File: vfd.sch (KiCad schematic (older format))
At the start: 35 parts, among them Q1 AO3400A, Q13 TO-252, Q14 CJT04N15, Q2 AO3400A, T1 Wuerth 760390013, T2 Wuerth 760390013, T3 Wuerth 760390013, T4 Wuerth 760390013, U1 SN74AVC8T245PW, U4 MN12864K

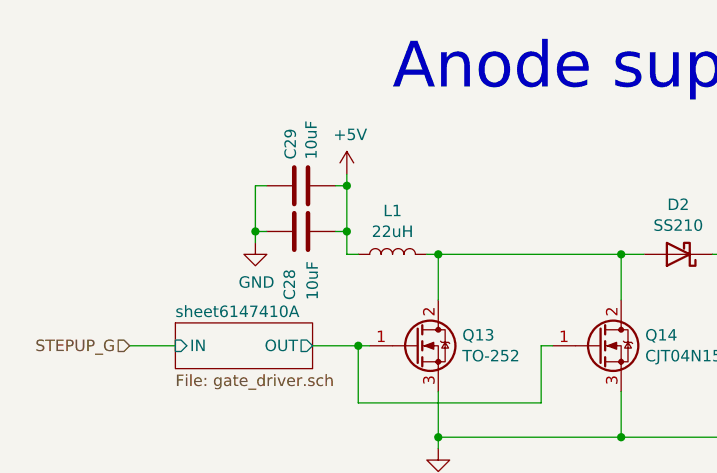
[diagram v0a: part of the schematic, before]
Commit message: Assign unique value to low voltage 0805 caps
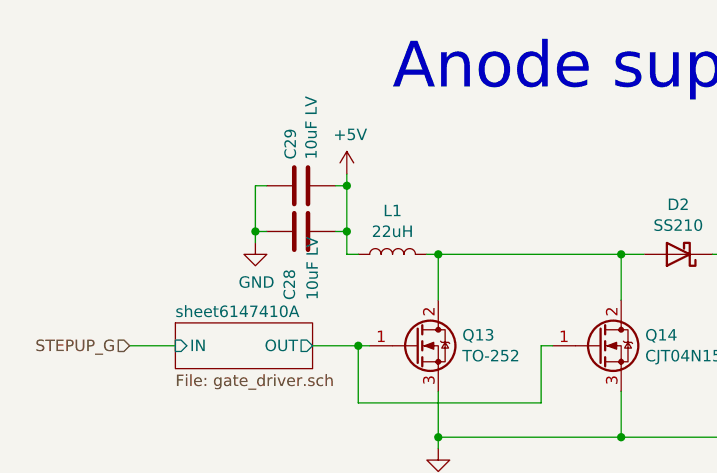
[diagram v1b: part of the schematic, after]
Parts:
- C28, C29: value 10uF -> 10uF LV
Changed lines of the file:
@@
-$Comp
-L Device:C C?
-U 1 1 60D56122
-P 2000 1450
-AR Path="/60B03476/60D3C691/60D56122" Ref="C?"  Part="1"
-AR Path="/60B03476/60D56122" Ref="C28"  Part="1"
-F 0 "C28" H 1700 1500 50  0000 L CNN
-F 1 "10uF" H 1700 1400 50  0000 L CNN
-F 2 "Capacitor_SMD:C_0805_2012Metric" H 2038 1300 50  0001 C CNN
-F 3 "~" H 2000 1450 50  0001 C CNN
-F 4 "C15850" V 2000 1450 50  0001 C CNN "LCSC"
-	1    2000 1450
-	0    -1   -1   0
-$EndComp
 $Comp
 L Device:C C?
@@
 AR Path="/60B03476/60D56129" Ref="C29"  Part="1"
 F 0 "C29" H 2115 1296 50  0000 L CNN
-F 1 "10uF" H 2115 1205 50  0000 L CNN
+F 1 "10uF LV" H 2115 1205 50  0000 L CNN
 F 2 "Capacitor_SMD:C_0805_2012Metric" H 2038 1100 50  0001 C CNN
 F 3 "~" H 2000 1250 50  0001 C CNN
@@
 Connection ~ 4750 1550
 Connection ~ 4750 2350
+$Comp
+L Device:C C?
+U 1 1 60D56122
+P 2000 1450
+AR Path="/60B03476/60D3C691/60D56122" Ref="C?"  Part="1"
+AR Path="/60B03476/60D56122" Ref="C28"  Part="1"
+F 0 "C28" H 1700 1500 50  0000 L CNN
+F 1 "10uF LV" H 1700 1400 50  0000 L CNN
+F 2 "Capacitor_SMD:C_0805_2012Metric" H 2038 1300 50  0001 C CNN
+F 3 "~" H 2000 1450 50  0001 C CNN
+F 4 "C15850" V 2000 1450 50  0001 C CNN "LCSC"
+	1    2000 1450
+	0    -1   -1   0
+$EndComp
 $EndSCHEMATC
